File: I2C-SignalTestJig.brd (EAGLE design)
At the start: 100 x 100 mm, 50 parts, among them CON1 1x4, CON2 1x4, CON3 1x4, CON4 1x4, CON5 1x4, CON6 1x4, IC1 74LS139D, IC2 74LS139D, IC3 74LS139D, IC4 MCP23017SO

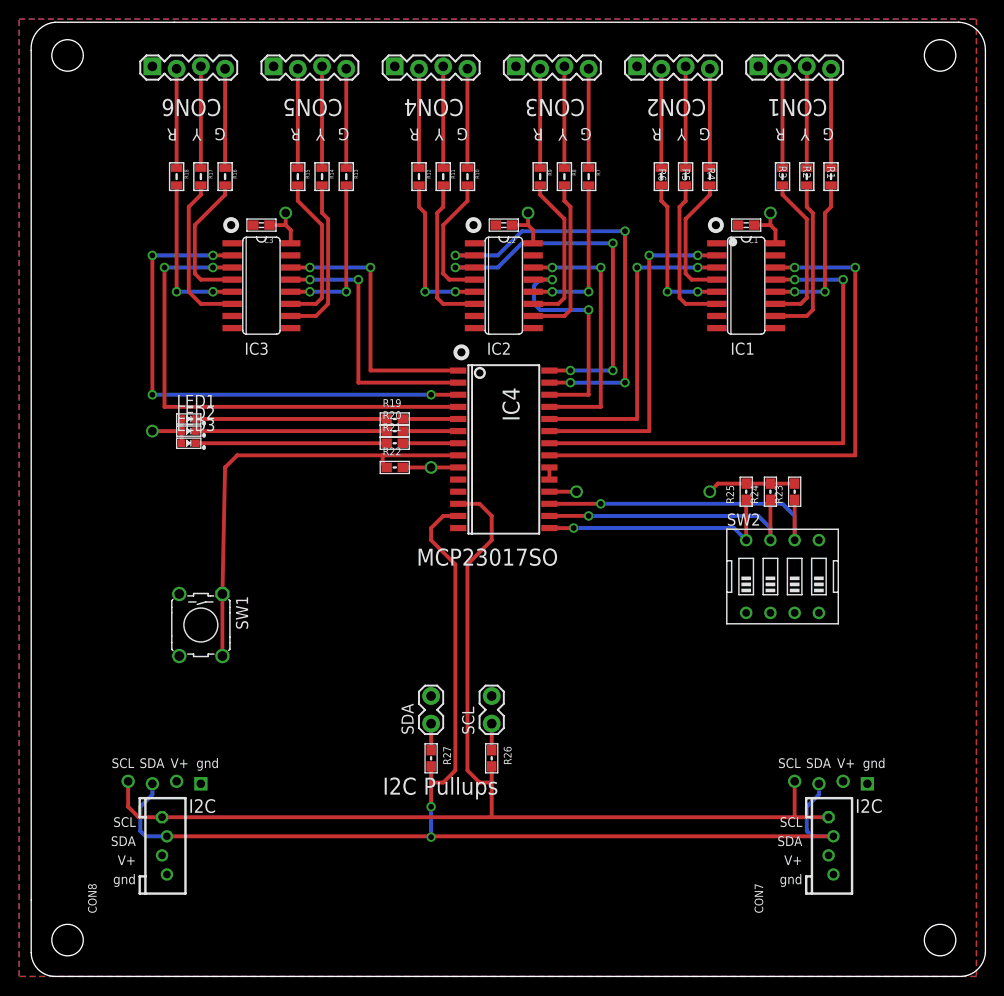
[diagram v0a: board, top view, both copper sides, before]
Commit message: added values for connectors
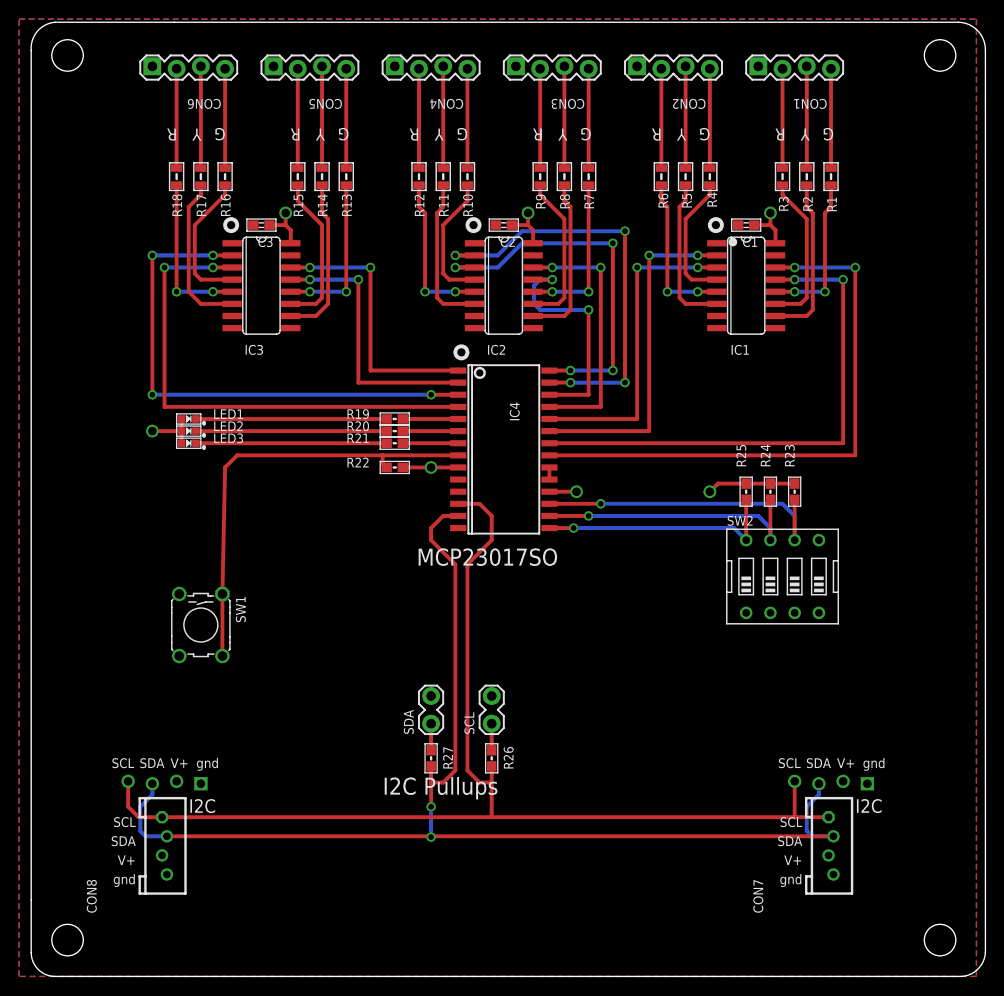
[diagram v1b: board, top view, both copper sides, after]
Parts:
- BOARD1: value (none) -> 10x10
- CON7, CON8: value (none) -> I2C
- SW1: value (none) -> SPST-MOM
- SW2: value (none) -> SPSTx4

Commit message: normalized values
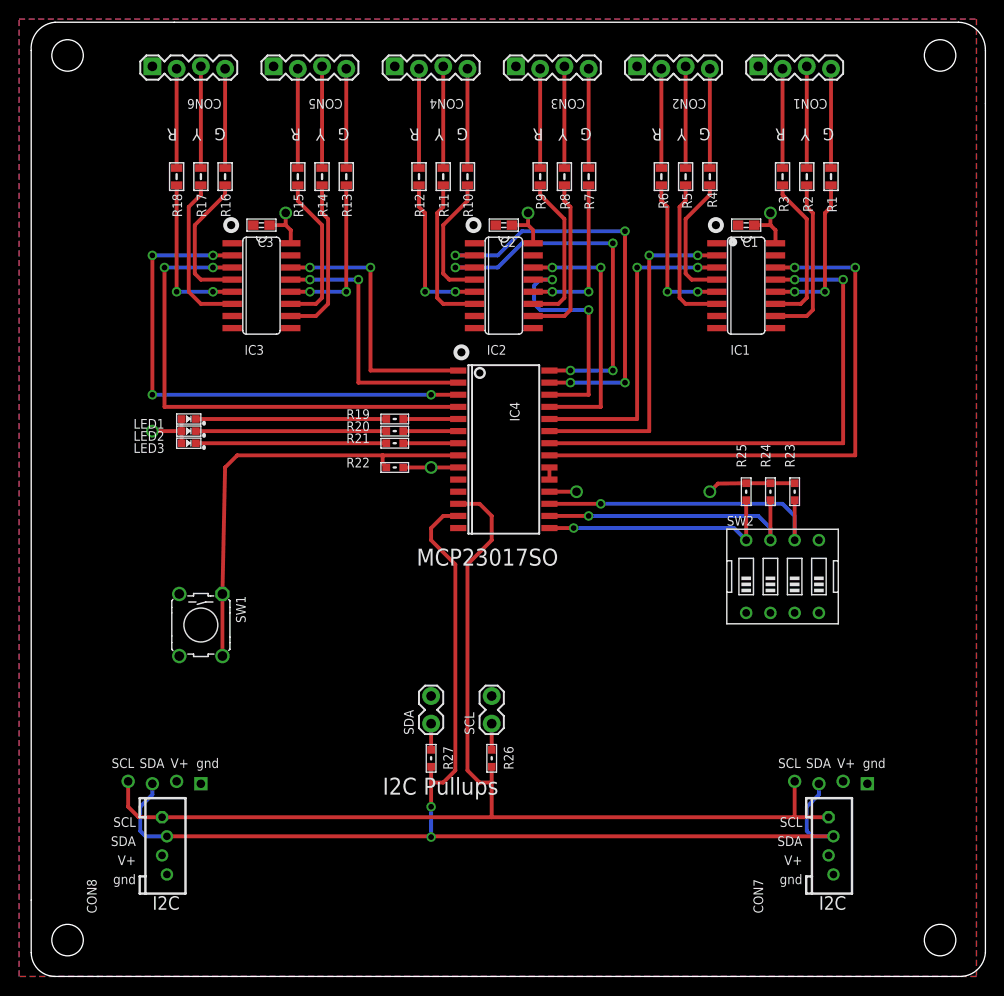
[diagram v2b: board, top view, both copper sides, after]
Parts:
- BOARD1: value 10x10 -> BOARD
- CON1, CON2, CON3, CON4, CON5, CON6: value 1x4 -> 0.100
- SCL: value SCL -> 0.100
- SDA: value SDA -> 0.100
- turned LED1 to 180 degrees
- turned LED2 to 180 degrees
- turned LED3 to 180 degrees
